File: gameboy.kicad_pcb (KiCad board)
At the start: 4 copper layers, 90 x 125 mm, 103 parts, among them J1 SM03B-SRSS-TB, J2 FPC-05F-12PH20, J3 Conn_01x02, J4 Conn_01x02, J5 Conn_01x02, J6 SD_Card_Receptacle, J7 USB_C_Receptacle_USB2.0_16P, Q1 SS8050, Q2 AO3401A, Q3 SS8050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

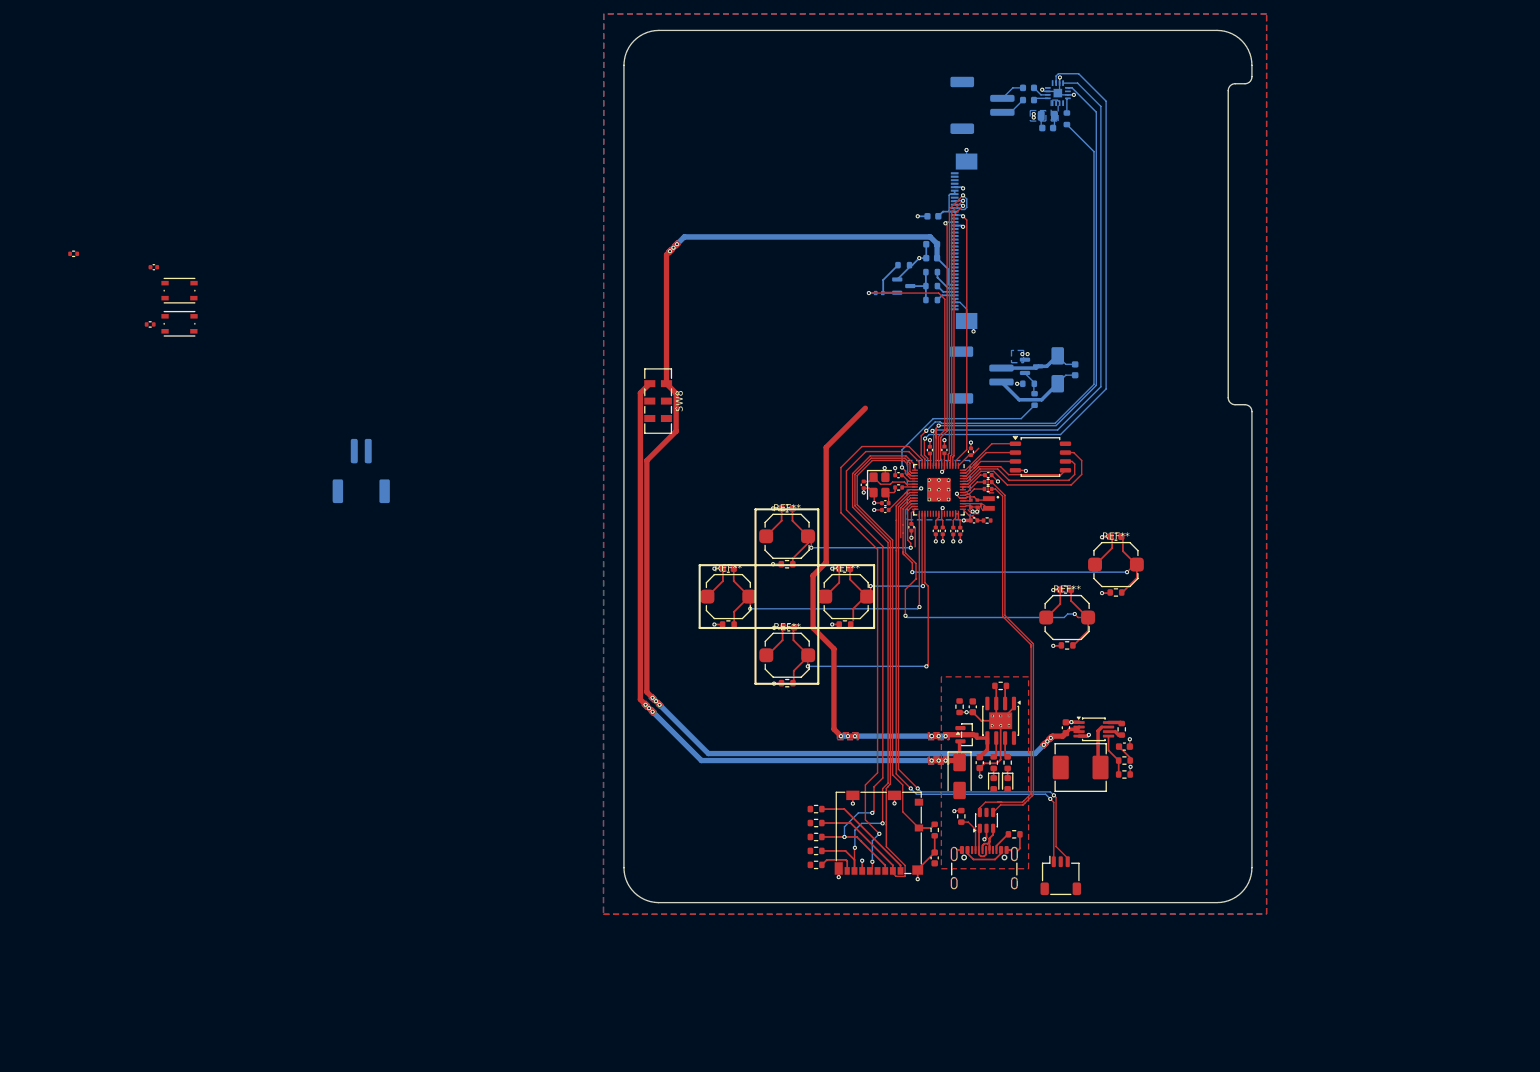
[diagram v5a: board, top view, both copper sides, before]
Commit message: overhaul mcu layout, add last components, stitching vias, run DRC
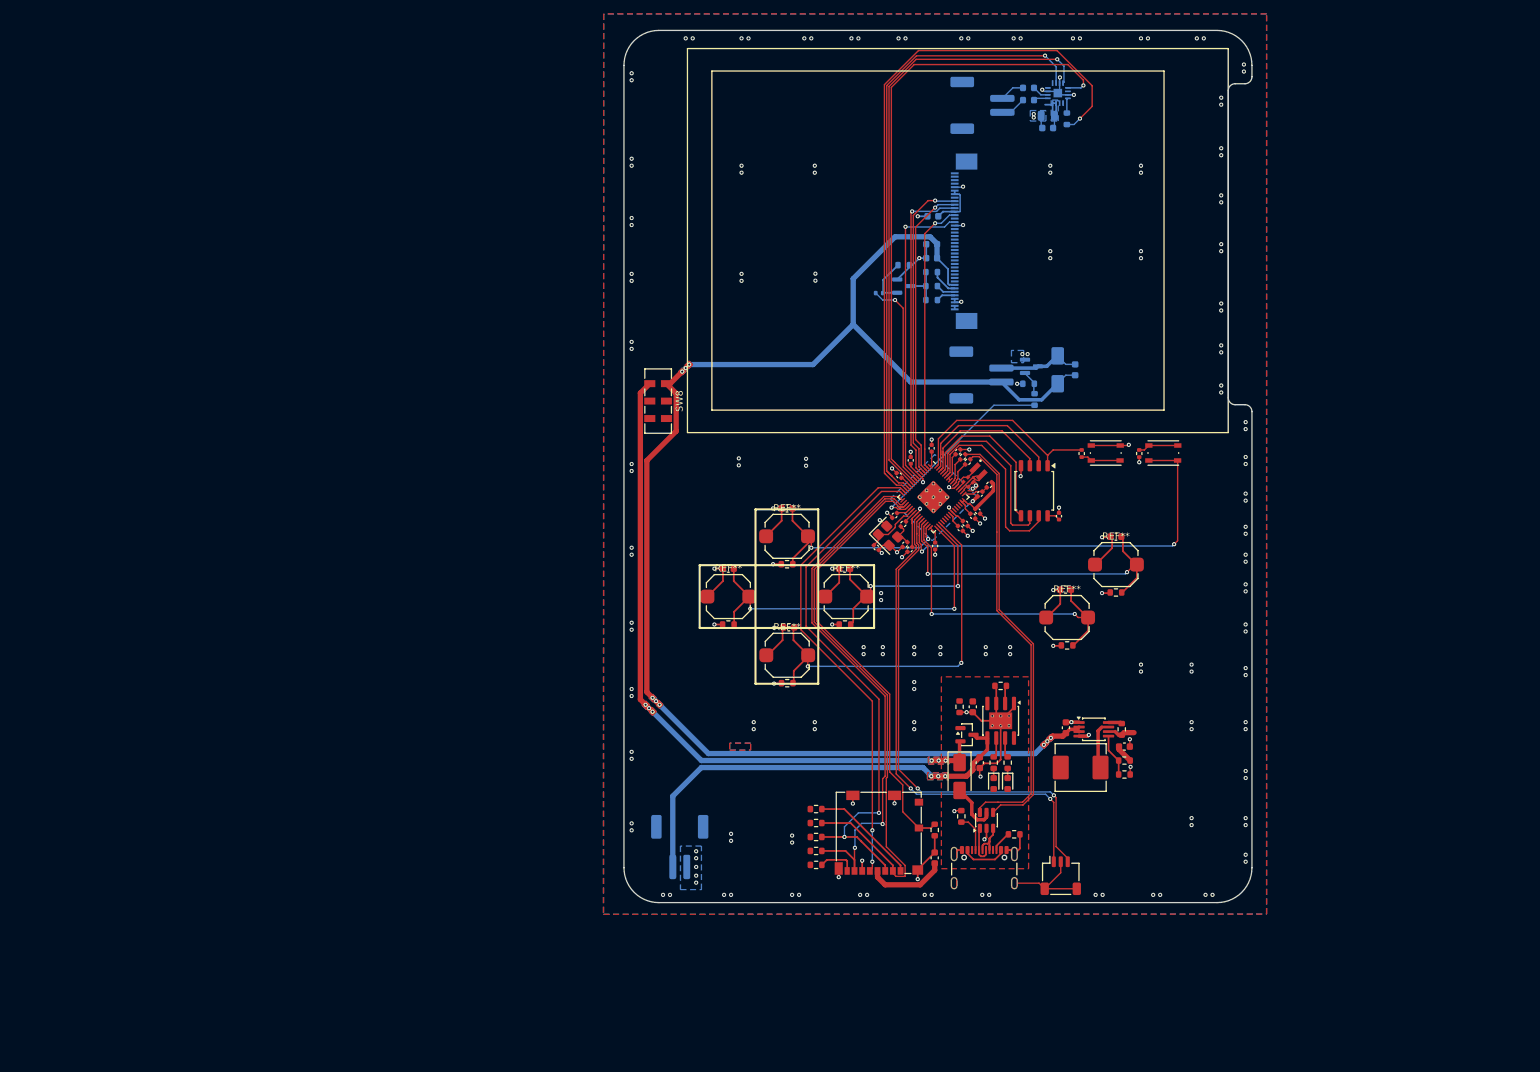
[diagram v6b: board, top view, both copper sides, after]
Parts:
- moved R3 155.4 mm to (172.8, 92.0), turned to -90 degrees
- moved SW1 142.9 mm to (176.2, 91.9)
- moved R6 134.8 mm to (164.5, 92.0), turned to -90 degrees
- moved C16 134.5 mm to (161.2, 101.0), turned to 90 degrees
- moved SW2 134.0 mm to (167.9, 91.9)
- moved J3 70.6 mm to (106.9, 148.4), turned to 0 degrees
- moved C2 9.16 mm to (135.1, 105.5), turned to -45 degrees
- moved Y1 7.39 mm to (136.7, 103.8), turned to -45 degrees
- moved C5 6.65 mm to (139.9, 105.7), turned to -135 degrees
- moved C3 6.56 mm to (139.2, 105.0), turned to -135 degrees
- moved C15 5.79 mm to (137.7, 100.9), turned to -135 degrees
- moved C11 5.73 mm to (138.3, 95.1), turned to 135 degrees
- moved C9 5.65 mm to (143.0, 91.2)
- moved C14 5.47 mm to (146.8, 91.8), turned to 45 degrees
- moved R2 5.28 mm to (138.9, 102.1), turned to -135 degrees
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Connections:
- J2 pad MP: GND -> unconnected-(J2-MountPin-PadMP)
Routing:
- net Net-(U1-RUN): track 6.88 -> 57.8 mm, vias 0 -> 2
- net /Audio/I2S_SDMODE: track 71.4 -> 101.4 mm
- net VDC: track 239.0 -> 213.7 mm
- net /MCU/QSPI_SS: track 9.10 -> 29.6 mm
- net /Power/BAT+: track 83.5 -> 65.4 mm, vias 7 -> 3
- net +3V3: track 50.6 -> 68.6 mm, vias 6 -> 83
- net /Audio/I2S_DIN: track 76.4 -> 90.9 mm
- net GND: track 138.6 -> 152.6 mm, vias 51 -> 135
- net /MCU/QSPI_SD1: track 9.27 -> 22.4 mm
- net /MCU/QSPI_SD2: track 9.65 -> 20.7 mm
- net /Audio/I2S_BCLK: track 78.8 -> 88.0 mm
- net /Buttons/BTN_B: track 54.8 -> 46.1 mm
- net /MCU/SD_CLK: track 76.6 -> 67.9 mm
- net /MCU/QSPI_SD0: track 16.2 -> 23.7 mm
- net /LCD/LCD_RST: track 36.7 -> 44.2 mm
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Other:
- board text added: "LCD"

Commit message: hide refs
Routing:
- net GND: track 152.6 -> 147.7 mm
- net +3V3: track 68.6 -> 67.0 mm
- net Net-(J4-Pin_1): track 3.69 -> 2.47 mm
- net /Power/USB_VBUS: track 14.7 -> 13.9 mm
- net /MCU/QSPI_SD2: track 20.7 -> 20.0 mm
- net /Buttons/BTN_UP: track 30.9 -> 30.1 mm
- net /LCD/LCD_BL: track 31.1 -> 30.4 mm
- net Net-(C3-Pad1): track 3.73 -> 3.07 mm
- net /MCU/QSPI_SD1: track 22.4 -> 21.9 mm
- net /MCU/SWD: track 71.7 -> 71.2 mm
